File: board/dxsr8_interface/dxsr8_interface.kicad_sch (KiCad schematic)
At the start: 11 parts, among them J1 RJ45, J2 RJ45, K1 Relay_DPDT, K2 Relay_DPDT, U1 PC817, U2 PC817, U3 PC817, U4 PC817

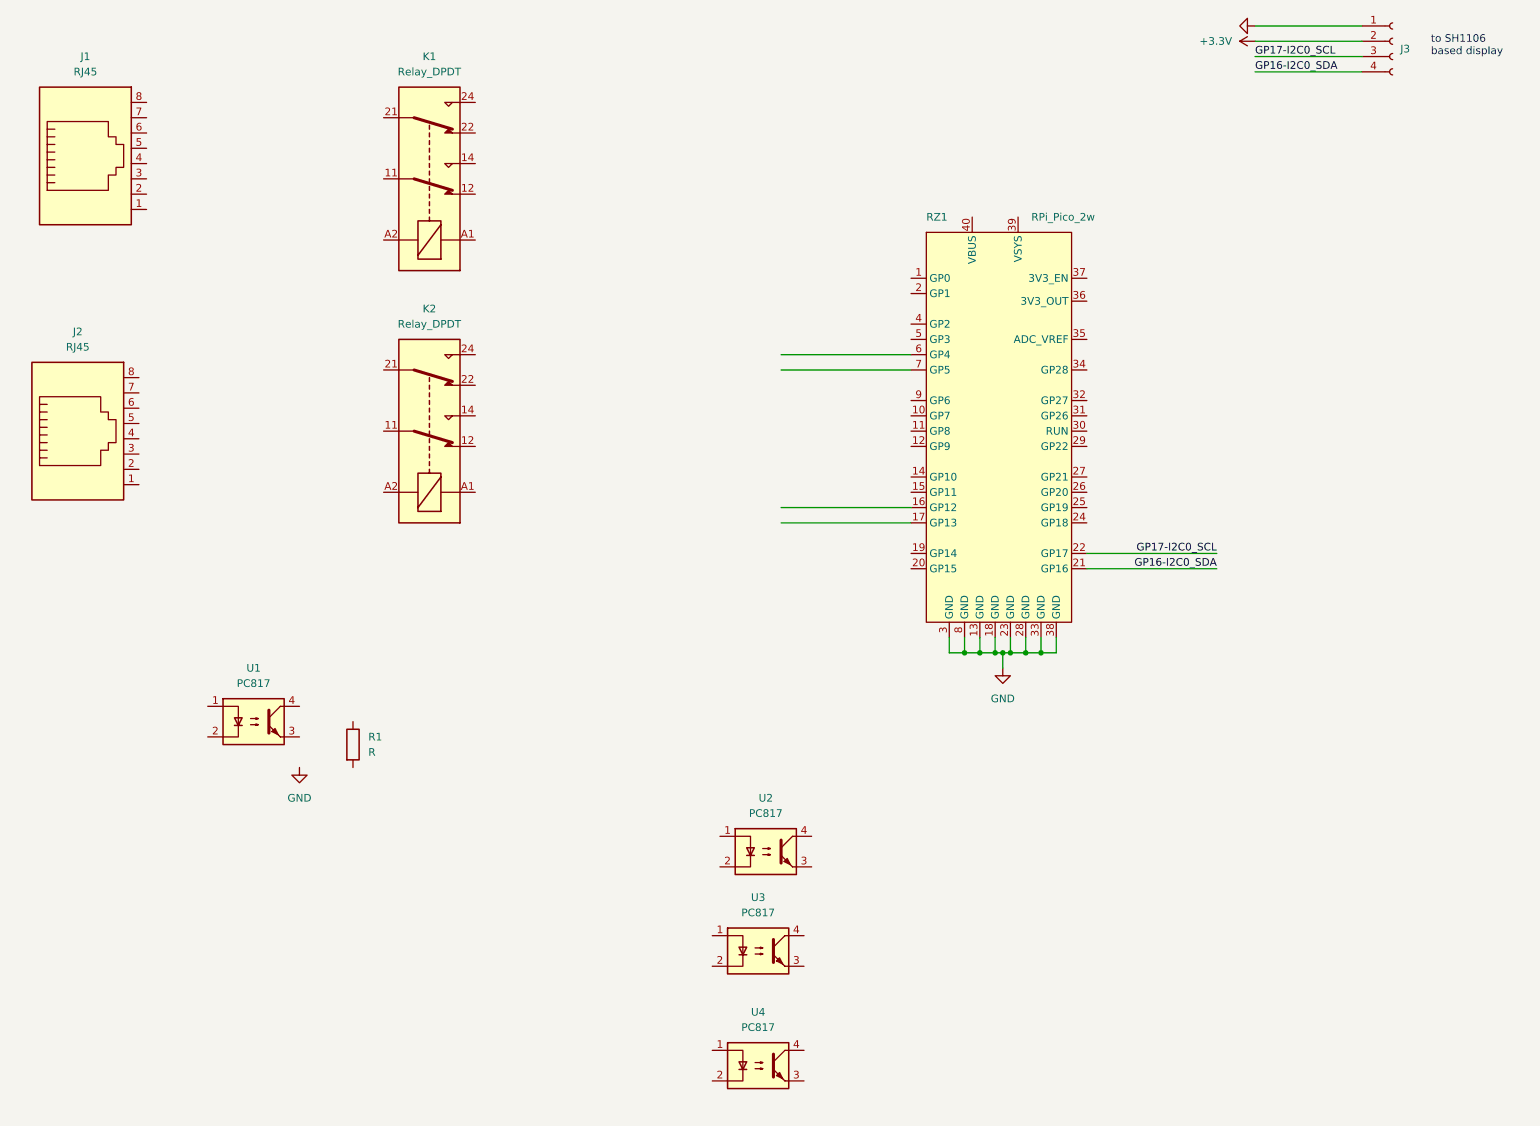
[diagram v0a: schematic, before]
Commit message: switch to ADM1201 isolators, add regulator for them
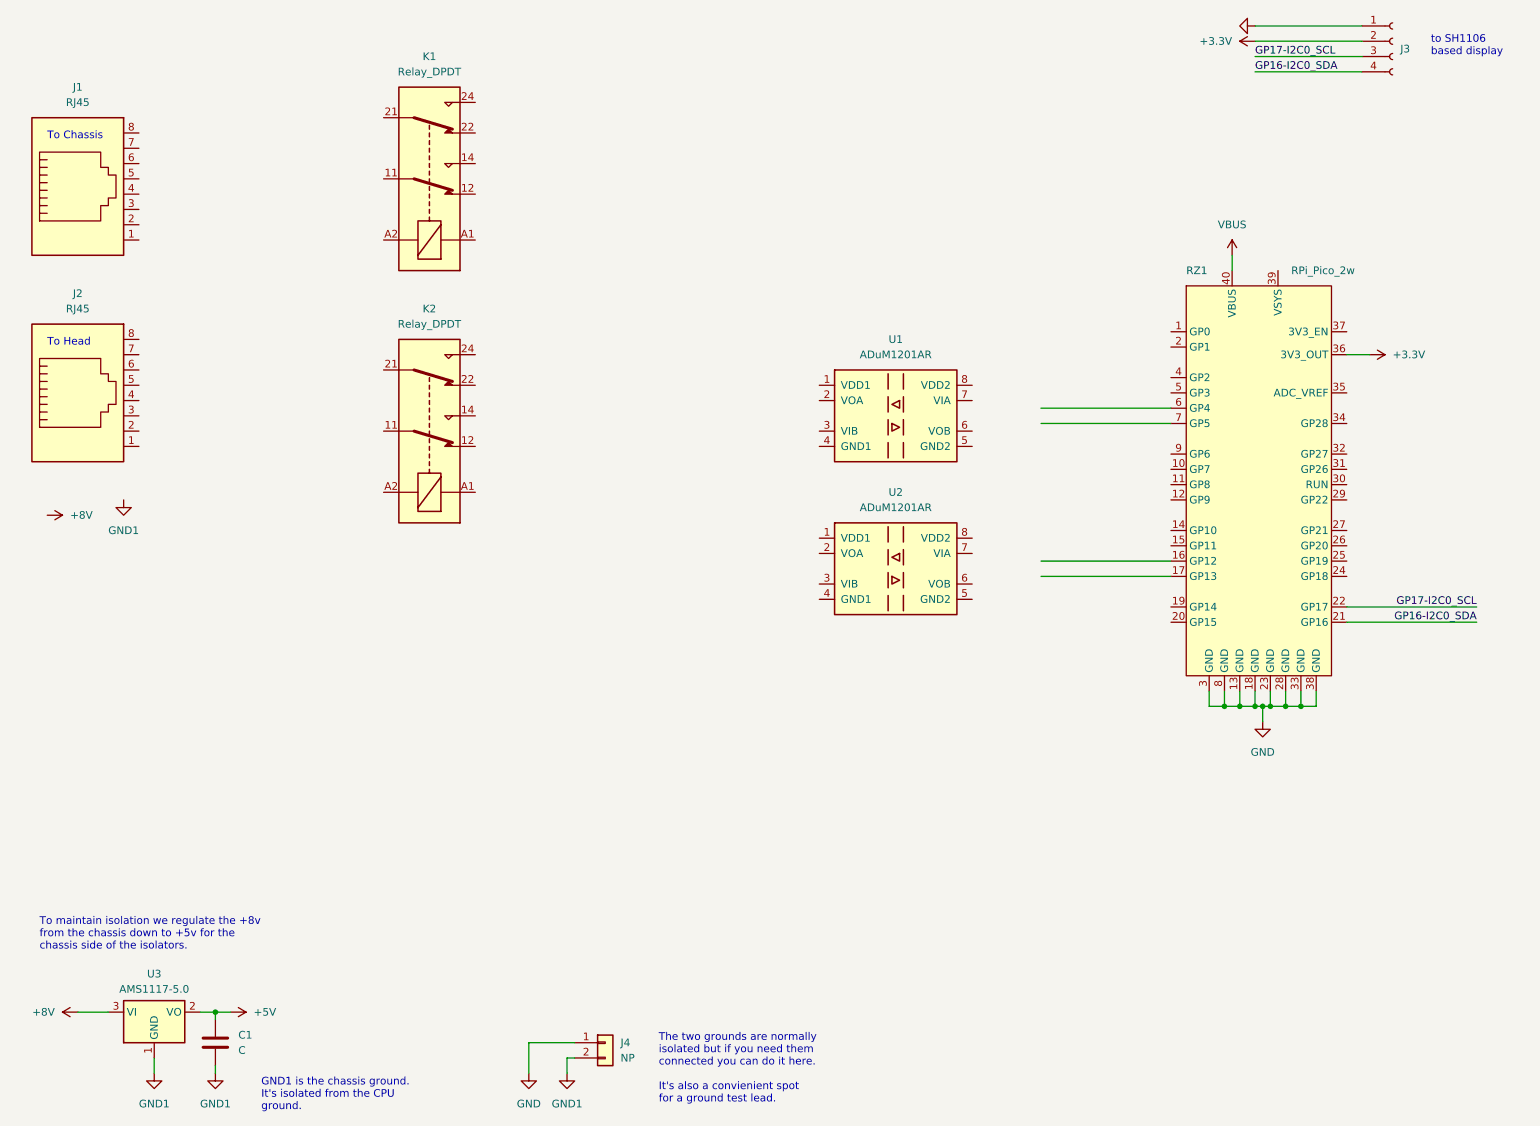
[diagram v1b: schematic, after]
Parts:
- removed R1: R, symbol Device:R
- removed U1, U2, U3, U4: PC817, Package_DIP:DIP-4_W7.62mm, symbol Isolator:PC817
- added C1: C, symbol Device:C
- added J4: NP, symbol Connector_Generic:Conn_01x02
- added U1, U2: ADuM1201AR, Package_SO:SOIC-8_3.9x4.9mm_P1.27mm, symbol Isolator:ADuM1201AR
- added U3: AMS1117-5.0, Package_TO_SOT_SMD:SOT-223-3_TabPin2, symbol Regulator_Linear:AMS1117-5.0
- renumbered J2 to J1, J1 to J2
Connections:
- net +3.3V: now also RZ1.36 (3V3_OUT)
- net GND: now also J4.1 (Pin_1)
- net VBUS: now reaches RZ1.40 (VBUS)
- new net +5V: C1.1, U3.2 (VO)
- new net +8V: U3.3 (VI)
- new net GND1: C1.2, J4.2 (Pin_2), U3.1 (GND)
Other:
- note added: "GND1 is the chassis ground. It's isolated from the CPU ground."
- note added: "The two grounds are normally isolated but if you need them connected you can do it here. It's also a convienient spot for a ground test lead."
- note added: "To Chassis"
- note added: "To Head"
- note added: "To maintain isolation we regulate the +8v from the chassis down to +5v for the chassis side of the isolators."
- moved on the sheet: J1, J2, RZ1

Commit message: work on board design
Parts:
- J1, J2: footprint (none) -> digikey-footprints:Ethernet_Jack_ARJC02-111008B; symbol Connector:RJ45 -> dk_Modular-Connectors-Jacks:RJLSE4208101T; Category (none) -> Connectors, Interconnects; DK_Datasheet_Link (none) -> https://cdn.amphenol-icc.com/media/wysiwyg/files/drawing/rj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; DK_Detail_Page (none) -> /product-detail/en/amphenol-icc-commercial-products/RJLSE42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; Digi-Key_PN (none) -> RJLSE4208101TTR-ND; Family (none) -> Modular Connectors - Jacks; MPN (none) -> RJLSE4208101T; Manufacturer (none) -> Amphenol ICC (Commercial Products); Status (none) -> Active
- J3: footprint (none) -> Connector_PinHeader_2.54mm:PinHeader_1x04_P2.54mm_Vertical
- J4: footprint (none) -> Connector_PinHeader_2.54mm:PinHeader_1x02_P2.54mm_Vertical
- K1, K2: value Relay_DPDT -> HK19F-DC3V-SHG; footprint (none) -> Relay_THT:Relay_DPDT_FRT5
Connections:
- net +3.3V: now also U1.8 (VDD2), U2.8 (VDD2)
- net +5V: now also U1.1 (VDD1), U2.1 (VDD1)
- net +8V: now also J1.3, J2.3
- net GND: now also K1.A2, K2.A2, U1.5 (GND2), U2.5 (GND2)
- net GND1: now also J1.6, J1.9, J2.6, J2.9, U1.4 (GND1), U2.4 (GND1)
- net GP16-I2C0_SDA: no longer RZ1.21 (GP16)
- net GP17-I2C0_SCL: no longer RZ1.22 (GP17)
- net UART0_TX: now reaches RZ1.16 (GP12)
- net UART0_RX: now reaches RZ1.17 (GP13)
- net RELAY_CTL: now reaches RZ1.29 (GP22)
- net UART1_TX: now reaches RZ1.6 (GP4)
- net UART1_RX: now reaches RZ1.7 (GP5)
- net CTXD: now reaches J1.1
- net CTXD: now also K1.21
- net CRXD: now reaches J1.2
- net CRXD: now also K1.11
- net CLN: now reaches J1.4
- net CLN: now also J2.4
- net MIC: now reaches J1.5
- net MIC: now also J2.5
- net SP: now reaches J1.7
- net SP: now also J2.7
- net SPG: now reaches J1.8
- net SPG: now also J2.8
- net HRXD: now reaches J2.1
- net HRXD: now also K2.21
- net HTXD: now reaches J2.2
- net HTXD: now also K2.11
- net RELAY: now reaches K1.A1
- net RELAY: now also K2.A1
- new net I2C0_SCL: RZ1.22 (GP17)
- new net I2C0_SDA: RZ1.21 (GP16)
- no-connect marks 0 -> 20
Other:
- note added: "Needs transistor to drive coil"
- moved on the sheet: K1, K2, RZ1, U1, U2
